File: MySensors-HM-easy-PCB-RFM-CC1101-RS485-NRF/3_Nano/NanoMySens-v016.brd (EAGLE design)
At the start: 25 x 36.8 mm, 34 parts, among them IC1 ATSHA204A, IC31 ATMEGA168-TQFP, U1 RFM69HCW, Y2 8MHZ

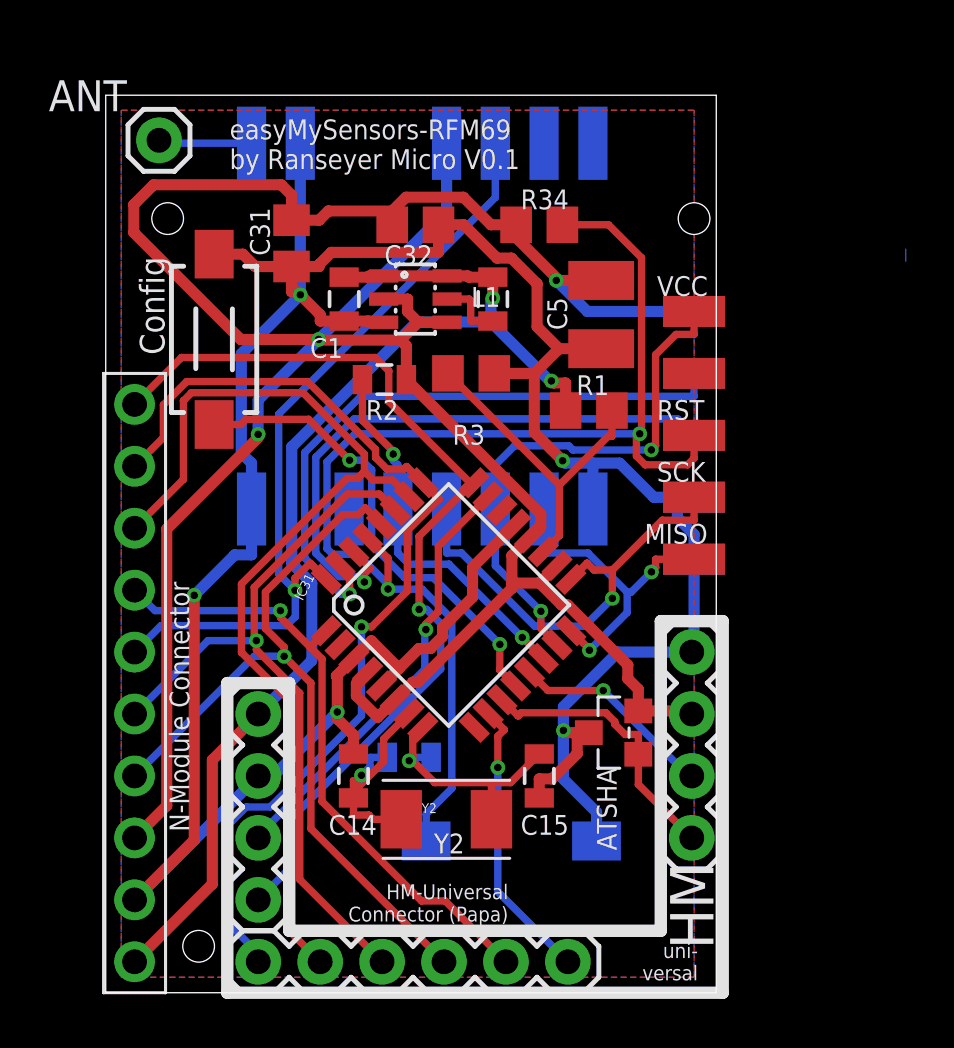
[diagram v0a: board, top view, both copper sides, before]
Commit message: Update RFM95
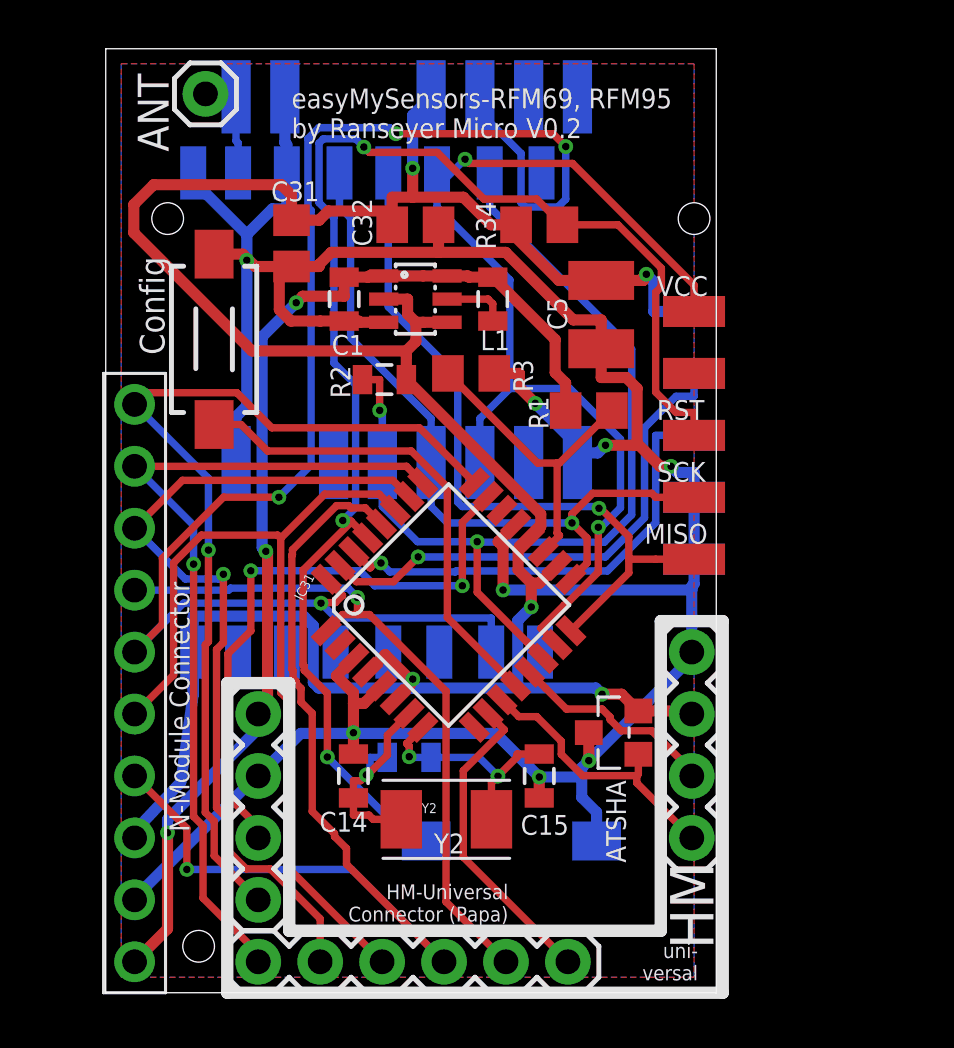
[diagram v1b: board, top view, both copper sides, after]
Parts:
- added RFM69W: RFM69HW, hoperf:RFM
- moved ANT 2.69 mm to (4.09, 36.9)
- moved U1 2.01 mm to (12.3, 29.2)
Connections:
- net ANT: now also RFM69W.ANT
- net D10_SS: now also RFM69W.NSS
- net D11_MOSI: now also RFM69W.MOSI
- net D12_MISO: now also RFM69W.MISO
- net D13_SCK: now also RFM69W.SCK
- net D2_INT0: now also RFM69W.DIO0
- net GND: now also RFM69W.GNDA, RFM69W.GNDB
- net VCC: now also RFM69W.VCC
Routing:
- net D2_INT0: track 32.9 -> 64.8 mm, vias 1 -> 4
- net D10_SS: track 15.5 -> 39.6 mm
- net D11_MOSI: track 22.0 -> 43.4 mm
- net D12_MISO: track 13.5 -> 31.6 mm, vias 2 -> 1
- net D13_SCK: track 18.7 -> 29.9 mm
- net A5: track 32.8 -> 41.0 mm
- net RESET: track 50.9 -> 58.8 mm, vias 2 -> 3
- net VCC: track 116.3 -> 108.8 mm, vias 3 -> 5
- net A0: track 17.9 -> 24.9 mm, vias 1 -> 2
- net GND: track 127.2 -> 120.5 mm, vias 5 -> 8
- net A2: track 40.9 -> 34.5 mm
- net A3: track 41.4 -> 35.3 mm, vias 0 -> 1
- net RXD: track 24.5 -> 18.9 mm
- net A4: track 31.4 -> 36.6 mm, vias 1 -> 0
- net TXD: track 26.0 -> 21.0 mm
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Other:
- board size 25 x 36.8 mm -> 25 x 38.7 mm
- board text added: "easyMySensors-RFM69, RFM95 by Ranseyer Micro V0.2"
- board text removed: "RFM69(H)W"
- board text removed: "X"
- board text removed: "easyMySensors-RFM69 by Ranseyer Micro V0.1"
